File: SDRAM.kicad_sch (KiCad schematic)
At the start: 31 parts, among them J1 Micro_SD_Card_Det_Hirose_DM3AT, U1 MT25Q, U11 MT48LC16M16A2P, U2 IS42S16160J-7TL, U7 CAT24C128, U9 W25Q128JVS

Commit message: LTDC route almost finished
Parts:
- removed C22: 100n, Capacitor_SMD:C_0402_1005Metric, symbol Device:C_Small
- removed R1: 10K, Resistor_SMD:R_0402_1005Metric, symbol Device:R_Small
- removed U2: IS42S16160J-7TL, Package_SO:TSOP-II-54_22.2x10.16mm_P0.8mm, symbol Memory_RAM:IS42S16400J-xC
- removed U9: W25Q128JVS, Package_SO:SOIC-8_5.23x5.23mm_P1.27mm, symbol Memory_Flash:W25Q128JVS
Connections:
- no-connect marks 3 -> 1
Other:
- note added: "C412833"
- note added: "or IS42S16160J-7TL"
- note removed: "NAND FLASH"
- note removed: "SDRAM"
- moved on the sheet: C18, C21, J1, R10, R2, R7, R8, R9, U1, U11

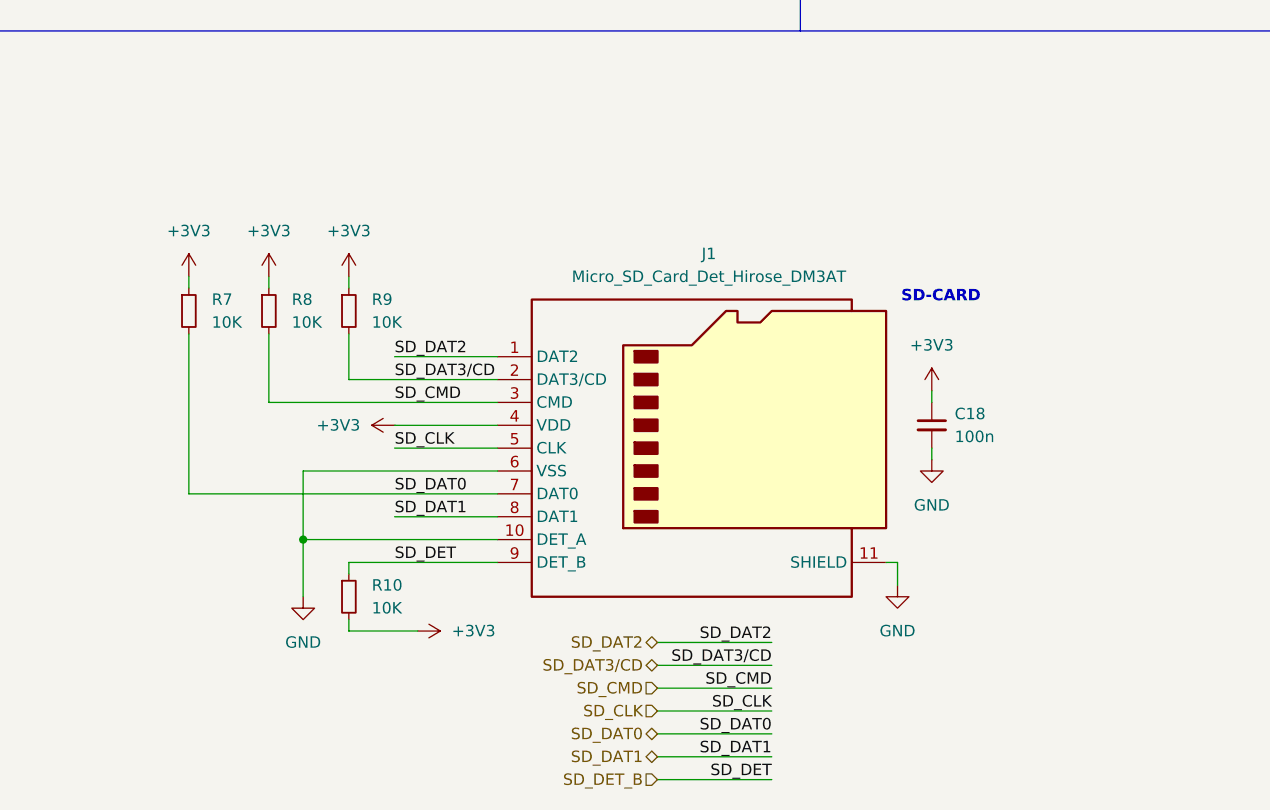
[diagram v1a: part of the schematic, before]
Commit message: Added chroma pixel png
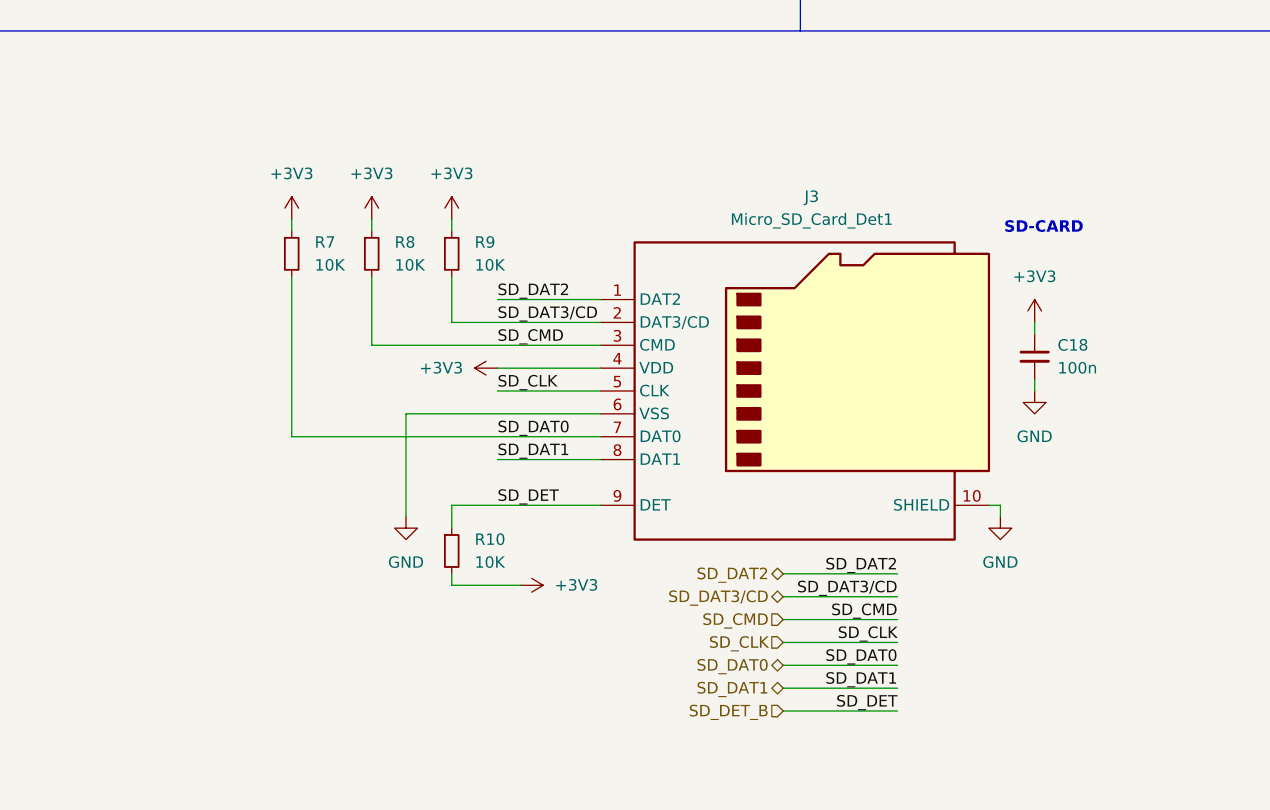
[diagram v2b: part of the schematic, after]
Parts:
- removed J1: Micro_SD_Card_Det_Hirose_DM3AT, Connector_Card:microSD_HC_Hirose_DM3AT-SF-PEJM5, symbol Connector:Micro_SD_Card_Det_Hirose_DM3AT
- added J3: Micro_SD_Card_Det1, TF-115:SD-TF-115, symbol Connector:Micro_SD_Card_Det1
- U11: JLCPCB Part # (none) -> C412833
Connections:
- net +3V3: now also J3.4 (VDD)
- net GND: now also J3.10 (SHIELD), J3.6 (VSS)
- net SD_CLK: now also J3.5 (CLK)
- net SD_CMD: now also J3.3 (CMD)
- net SD_DAT0: now also J3.7 (DAT0)
- net SD_DAT1: now also J3.8 (DAT1)
- net SD_DAT2: now also J3.1 (DAT2)
- net SD_DAT3/CD: now also J3.2 (DAT3/CD)
- net SD_DET_B: now also J3.9 (DET)
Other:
- moved on the sheet: C18, R10, R7, R8, R9
